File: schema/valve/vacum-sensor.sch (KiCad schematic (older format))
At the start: 6 parts, among them Q3 bc857, U3 PHDARL

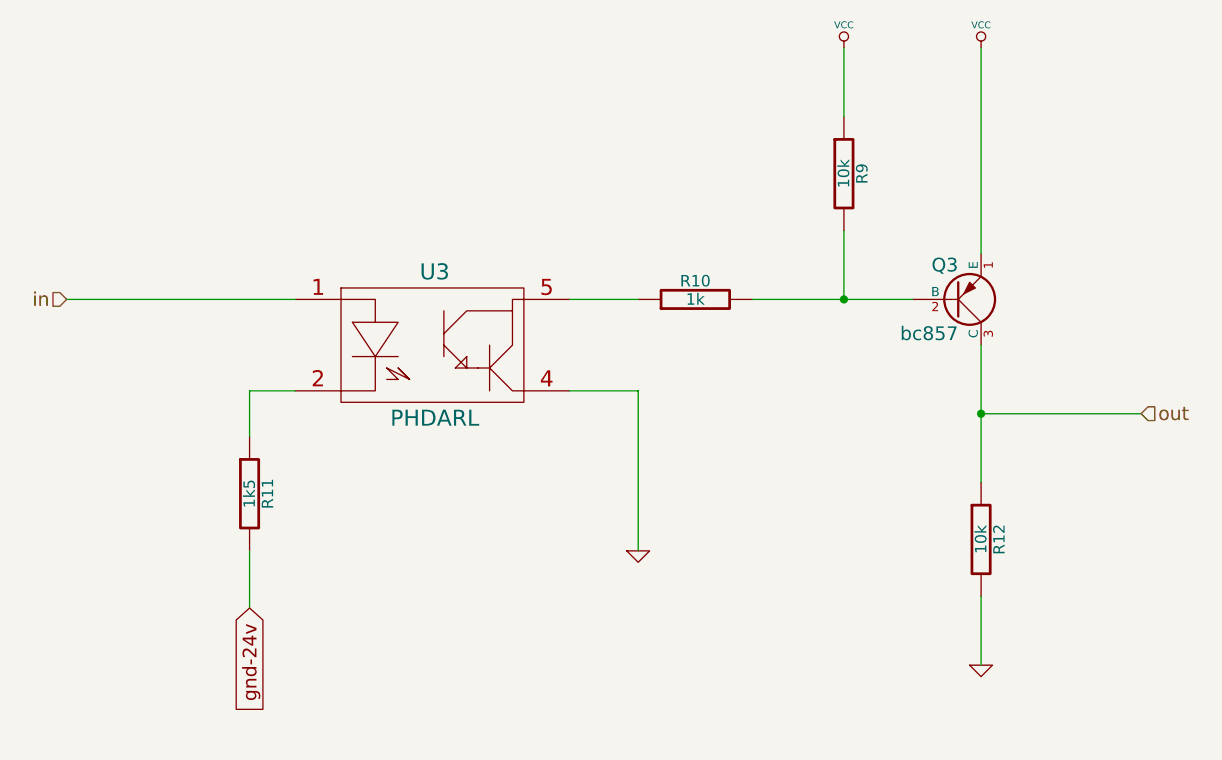
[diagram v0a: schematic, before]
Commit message: Added filtering capacitors.
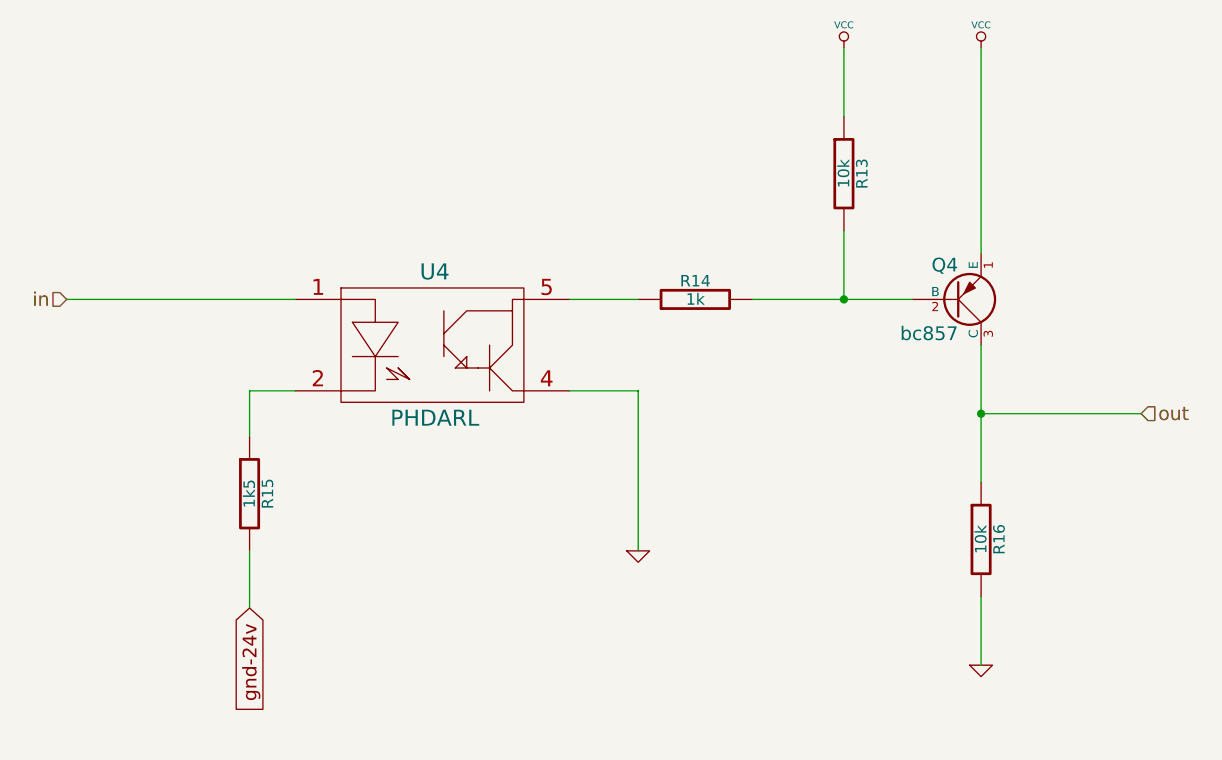
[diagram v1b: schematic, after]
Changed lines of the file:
@@
-EESchema Schematic File Version 2  date Tue 03 Apr 2012 12:20:51 AM MSK
+EESchema Schematic File Version 2  date Tue 03 Apr 2012 01:04:14 AM MSK
 LIBS:power
 LIBS:device
@@
 $Descr A4 11700 8267
 encoding utf-8
-Sheet 4 45
+Sheet 28 45
 Title ""
 Date "2 apr 2012"
@@
 AR Path="/4F79FC32/4F79F12A" Ref="#PWR28"  Part="1"
 AR Path="/4F79EEDB/4F79F12A" Ref="#PWR67"  Part="1"
-F 0 "#PWR12" H 7900 5100 30  0001 C CNN
+AR Path="/4F79FEFF/4F79F12A" Ref="#PWR12"  Part="1"
+AR Path="/4F79FF1E/4F79F12A" Ref="#PWR12"  Part="1"
+F 0 "#PWR16" H 7900 5100 30  0001 C CNN
 F 1 "GND" H 7900 5030 30  0001 C CNN
 	1    7900 5100
@@
 AR Path="/4F79FC32/4F79F111" Ref="R28"  Part="1"
 AR Path="/4F79EEDB/4F79F111" Ref="R91"  Part="1"
-F 0 "R12" V 7980 4550 50  0000 C CNN
+AR Path="/4F79FEFF/4F79F111" Ref="R12"  Part="1"
+AR Path="/4F79FF1E/4F79F111" Ref="R12"  Part="1"
+F 0 "R16" V 7980 4550 50  0000 C CNN
 F 1 "10k" V 7900 4550 50  0000 C CNN
 	1    7900 4550
@@
 AR Path="/4F79FC32/4F79F0F0" Ref="#PWR27"  Part="1"
 AR Path="/4F79EEDB/4F79F0F0" Ref="#PWR66"  Part="1"
-F 0 "#PWR11" H 6400 4600 30  0001 C CNN
+AR Path="/4F79FEFF/4F79F0F0" Ref="#PWR11"  Part="1"
+AR Path="/4F79FF1E/4F79F0F0" Ref="#PWR11"  Part="1"
+F 0 "#PWR15" H 6400 4600 30  0001 C CNN
 F 1 "GND" H 6400 4530 30  0001 C CNN
 	1    6400 4600
@@
 AR Path="/4F79FC32/4F79F0DB" Ref="#PWR26"  Part="1"
 AR Path="/4F79EEDB/4F79F0DB" Ref="#PWR65"  Part="1"
-F 0 "#PWR10" H 7900 2500 30  0001 C CNN
+AR Path="/4F79FEFF/4F79F0DB" Ref="#PWR10"  Part="1"
+AR Path="/4F79FF1E/4F79F0DB" Ref="#PWR10"  Part="1"
+F 0 "#PWR14" H 7900 2500 30  0001 C CNN
 F 1 "VCC" H 7900 2500 30  0000 C CNN
 	1    7900 2400
@@
 AR Path="/4F79FC32/4F79F0CE" Ref="#PWR25"  Part="1"
 AR Path="/4F79EEDB/4F79F0CE" Ref="#PWR64"  Part="1"
-F 0 "#PWR9" H 7300 2500 30  0001 C CNN
+AR Path="/4F79FEFF/4F79F0CE" Ref="#PWR9"  Part="1"
+AR Path="/4F79FF1E/4F79F0CE" Ref="#PWR9"  Part="1"
+F 0 "#PWR13" H 7300 2500 30  0001 C CNN
 F 1 "VCC" H 7300 2500 30  0000 C CNN
 	1    7300 2400
@@
 AR Path="/4F79FC32/4F79F09F" Ref="Q7"  Part="1"
 AR Path="/4F79EEDB/4F79F09F" Ref="Q30"  Part="1"
-F 0 "Q3" H 7800 3350 60  0000 R CNN
+AR Path="/4F79FEFF/4F79F09F" Ref="Q3"  Part="1"
+AR Path="/4F79FF1E/4F79F09F" Ref="Q3"  Part="1"
+F 0 "Q4" H 7800 3350 60  0000 R CNN
 F 1 "bc857" H 7800 3650 60  0000 R CNN
 	1    7800 3500
@@
 AR Path="/4F79FC32/4F79EFBA" Ref="R25"  Part="1"
 AR Path="/4F79EEDB/4F79EFBA" Ref="R88"  Part="1"
-F 0 "R9" V 7380 2950 50  0000 C CNN
+AR Path="/4F79FEFF/4F79EFBA" Ref="R9"  Part="1"
+AR Path="/4F79FF1E/4F79EFBA" Ref="R9"  Part="1"
+F 0 "R13" V 7380 2950 50  0000 C CNN
 F 1 "10k" V 7300 2950 50  0000 C CNN
 	1    7300 2950
@@
 AR Path="/4F79FC32/4F79EFB2" Ref="R26"  Part="1"
 AR Path="/4F79EEDB/4F79EFB2" Ref="R89"  Part="1"
-F 0 "R10" V 6730 3500 50  0000 C CNN
+AR Path="/4F79FEFF/4F79EFB2" Ref="R10"  Part="1"
+AR Path="/4F79FF1E/4F79EFB2" Ref="R10"  Part="1"
+F 0 "R14" V 6730 3500 50  0000 C CNN
 F 1 "1k" V 6650 3500 50  0000 C CNN
 	1    6650 3500
@@
 AR Path="/4F79FC32/4F79EF52" Ref="R27"  Part="1"
 AR Path="/4F79EEDB/4F79EF52" Ref="R90"  Part="1"
-F 0 "R11" V 4780 4350 50  0000 C CNN
+AR Path="/4F79FEFF/4F79EF52" Ref="R11"  Part="1"
+AR Path="/4F79FF1E/4F79EF52" Ref="R11"  Part="1"
+F 0 "R15" V 4780 4350 50  0000 C CNN
 F 1 "1k5" V 4700 4350 50  0000 C CNN
 	1    4700 4350
@@
 AR Path="/4F79FC32/4F79EF18" Ref="U7"  Part="1"
 AR Path="/4F79EEDB/4F79EF18" Ref="U18"  Part="1"
-F 0 "U3" H 5510 4020 70  0000 C CNN
+AR Path="/4F79FEFF/4F79EF18" Ref="U3"  Part="1"
+AR Path="/4F79FF1E/4F79EF18" Ref="U3"  Part="1"
+F 0 "U4" H 5510 4020 70  0000 C CNN
 F 1 "PHDARL" H 5510 3380 70  0000 C CNN
 	1    5500 3700

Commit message: Signed-off-by: z80 <litedictteam@gmail.com>
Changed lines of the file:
@@
-EESchema Schematic File Version 2  date Tue 03 Apr 2012 01:04:14 AM MSK
+EESchema Schematic File Version 2  date Tue 03 Apr 2012 09:00:56 PM MSK
 LIBS:power
 LIBS:device
@@
 $Descr A4 11700 8267
 encoding utf-8
-Sheet 28 45
+Sheet 27 28
 Title ""
-Date "2 apr 2012"
+Date "3 apr 2012"
 Rev ""
 Comp ""
@@
 AR Path="/4F79FEFF/4F79F12A" Ref="#PWR12"  Part="1"
 AR Path="/4F79FF1E/4F79F12A" Ref="#PWR12"  Part="1"
-F 0 "#PWR16" H 7900 5100 30  0001 C CNN
+F 0 "#PWR12" H 7900 5100 30  0001 C CNN
 F 1 "GND" H 7900 5030 30  0001 C CNN
 	1    7900 5100
@@
 AR Path="/4F79FEFF/4F79F111" Ref="R12"  Part="1"
 AR Path="/4F79FF1E/4F79F111" Ref="R12"  Part="1"
-F 0 "R16" V 7980 4550 50  0000 C CNN
+F 0 "R12" V 7980 4550 50  0000 C CNN
 F 1 "10k" V 7900 4550 50  0000 C CNN
 	1    7900 4550
@@
 AR Path="/4F79FEFF/4F79F0F0" Ref="#PWR11"  Part="1"
 AR Path="/4F79FF1E/4F79F0F0" Ref="#PWR11"  Part="1"
-F 0 "#PWR15" H 6400 4600 30  0001 C CNN
+F 0 "#PWR11" H 6400 4600 30  0001 C CNN
 F 1 "GND" H 6400 4530 30  0001 C CNN
 	1    6400 4600
@@
 AR Path="/4F79FEFF/4F79F0DB" Ref="#PWR10"  Part="1"
 AR Path="/4F79FF1E/4F79F0DB" Ref="#PWR10"  Part="1"
-F 0 "#PWR14" H 7900 2500 30  0001 C CNN
+F 0 "#PWR10" H 7900 2500 30  0001 C CNN
 F 1 "VCC" H 7900 2500 30  0000 C CNN
 	1    7900 2400
@@
 AR Path="/4F79FEFF/4F79F0CE" Ref="#PWR9"  Part="1"
 AR Path="/4F79FF1E/4F79F0CE" Ref="#PWR9"  Part="1"
-F 0 "#PWR13" H 7300 2500 30  0001 C CNN
+F 0 "#PWR9" H 7300 2500 30  0001 C CNN
 F 1 "VCC" H 7300 2500 30  0000 C CNN
 	1    7300 2400
@@
 AR Path="/4F79FEFF/4F79F09F" Ref="Q3"  Part="1"
 AR Path="/4F79FF1E/4F79F09F" Ref="Q3"  Part="1"
-F 0 "Q4" H 7800 3350 60  0000 R CNN
+F 0 "Q3" H 7800 3350 60  0000 R CNN
 F 1 "bc857" H 7800 3650 60  0000 R CNN
 	1    7800 3500
@@
 AR Path="/4F79FEFF/4F79EFBA" Ref="R9"  Part="1"
 AR Path="/4F79FF1E/4F79EFBA" Ref="R9"  Part="1"
-F 0 "R13" V 7380 2950 50  0000 C CNN
+F 0 "R9" V 7380 2950 50  0000 C CNN
 F 1 "10k" V 7300 2950 50  0000 C CNN
 	1    7300 2950
@@
 AR Path="/4F79FEFF/4F79EFB2" Ref="R10"  Part="1"
 AR Path="/4F79FF1E/4F79EFB2" Ref="R10"  Part="1"
-F 0 "R14" V 6730 3500 50  0000 C CNN
+F 0 "R10" V 6730 3500 50  0000 C CNN
 F 1 "1k" V 6650 3500 50  0000 C CNN
 	1    6650 3500
@@
 AR Path="/4F79FEFF/4F79EF52" Ref="R11"  Part="1"
 AR Path="/4F79FF1E/4F79EF52" Ref="R11"  Part="1"
-F 0 "R15" V 4780 4350 50  0000 C CNN
+F 0 "R11" V 4780 4350 50  0000 C CNN
 F 1 "1k5" V 4700 4350 50  0000 C CNN
 	1    4700 4350
@@
 AR Path="/4F79FEFF/4F79EF18" Ref="U3"  Part="1"
 AR Path="/4F79FF1E/4F79EF18" Ref="U3"  Part="1"
-F 0 "U4" H 5510 4020 70  0000 C CNN
+F 0 "U3" H 5510 4020 70  0000 C CNN
 F 1 "PHDARL" H 5510 3380 70  0000 C CNN
 	1    5500 3700

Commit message: Schema, svg and png.
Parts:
- renumbered Q3 to Q1, R11 to R1, R10 to R2, R9 to R3, R12 to R4, U3 to U1
